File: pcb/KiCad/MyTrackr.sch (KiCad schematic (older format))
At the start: 41 parts, among them CN1 GPS_ANTENNA, CON1 MICRO_SD, J1 REGULATOR_3V3, J2 CONN_ICSP, J3 CONN_SERIAL, J4 CONN_BAT, P1 CONN_OLED, Q1 Q_PMOS_GSD, SW1 BTN_RESET, SW2 BTN_BACK, SW3 BTN_PREV, SW4 BTN_NEXT, SW5 BTN_SEL, U1 ATmega328P-AU, U2 GPS-NEO-6M, U3 24AA32

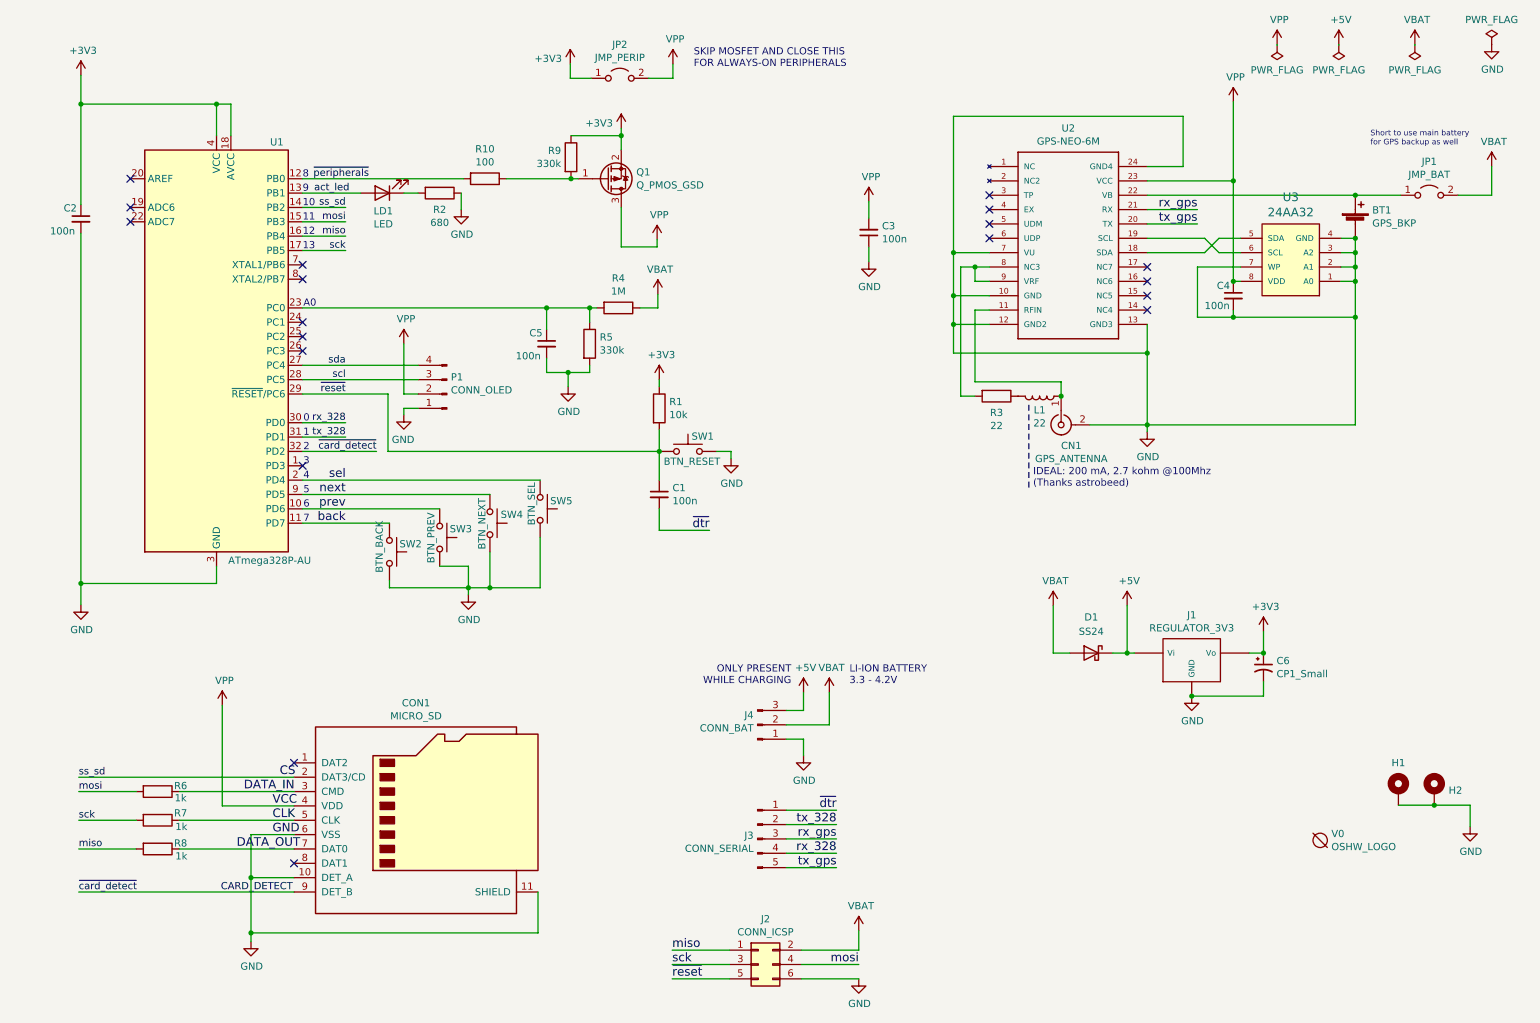
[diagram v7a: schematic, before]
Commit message: Add i2c pull-ups
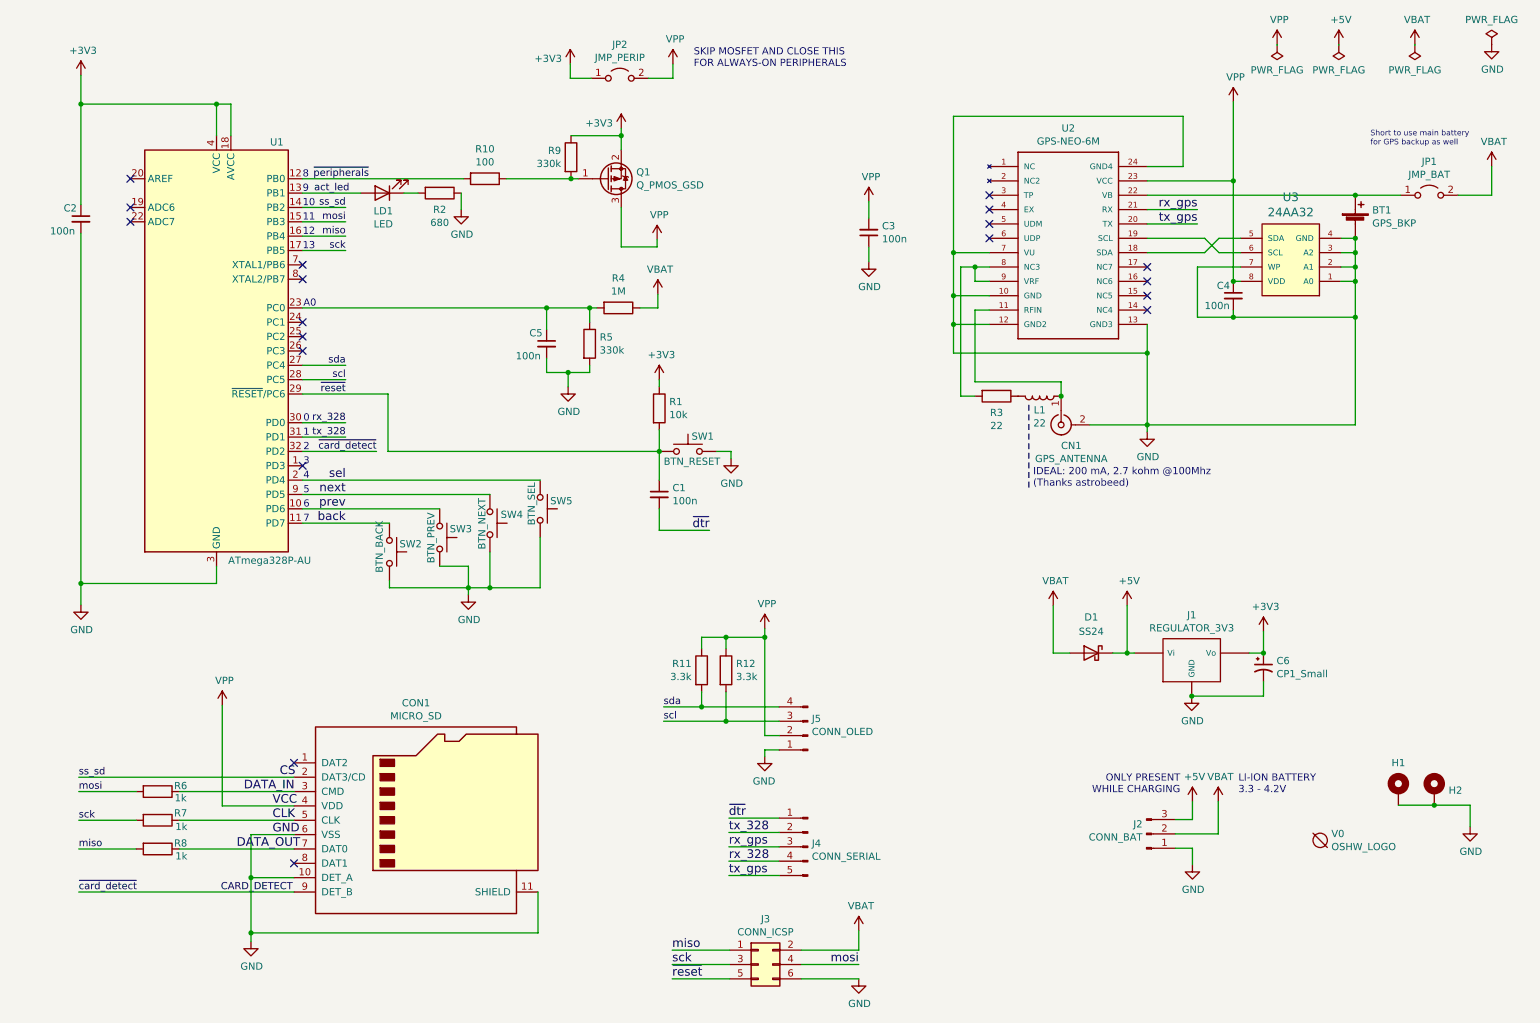
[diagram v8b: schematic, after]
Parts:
- added R11, R12: 3.3k, Resistor_SMD:R_0805_2012Metric_Pad1.20x1.40mm_HandSolder, symbol Device:R
- renumbered J4 to J2, J2 to J3, J3 to J4, P1 to J5
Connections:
- net VPP: now also R11.1, R12.1
- net scl: now also R12.2
- net sda: now also R11.2
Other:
- moved on the sheet: J2, J4, J5
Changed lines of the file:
@@
 Sheet 1 1
 Title "MyTrackr"
-Date "2021-01-10"
+Date "2021-01-14"
 Rev "2git"
 Comp "SukkoPera"
@@
 Text Label 8900 2050 2    60   ~ 0
 tx_gps
-Text Label 6385 6535 2    60   ~ 0
-tx_gps
-Text Label 6385 6435 2    60   ~ 0
-rx_328
-Text Label 6385 6335 2    60   ~ 0
-rx_gps
-Text Label 6385 6235 2    60   ~ 0
-tx_328
 Text Label 5500 4185 2    60   ~ 0
-~dtr
-Text Label 6385 6135 2    60   ~ 0
 ~dtr
 Text Label 2745 1835 0    50   ~ 0
@@
 	1505 6205 1105 6205
 Wire Wire Line
-	6385 6135 6035 6135
-Wire Wire Line
 	8550 2050 8900 2050
 Wire Wire Line
@@
 Wire Wire Line
 	4665 2635 4665 2735
-Wire Wire Line
-	3370 3335 3470 3335
 Connection ~ 10000 2700
 Connection ~ 5150 3635
@@
 	5150 4035 5150 4185
 Wire Wire Line
-	6385 6535 6035 6535
-Wire Wire Line
-	6385 6435 6035 6435
-Wire Wire Line
-	6385 6335 6035 6335
-Wire Wire Line
-	6385 6235 6035 6235
-Wire Wire Line
 	9360 5040 9360 4890
 Wire Wire Line
@@
 Wire Wire Line
 	2605 6305 2305 6305
-Wire Wire Line
-	3370 2885 3370 3235
 Wire Wire Line
 	1120 2115 1120 4555
@@
 $EndComp
 $Comp
-L Connector:Conn_01x03_Male J4
-U 1 1 60013045
-P 5835 5540
-F 0 "J4" H 5807 5472 50  0000 R CNN
-F 1 "CONN_BAT" H 5807 5563 50  0000 R CNN
-F 2 "Connector_PinHeader_2.54mm:PinHeader_1x03_P2.54mm_Vertical" H 5835 5540 50  0001 C CNN
-F 3 "~" H 5835 5540 50  0001 C CNN
-	1    5835 5540
-	1    0    0    1
-$EndComp
-$Comp
 L power:GND #PWR0106
 U 1 1 6003CA1E
@@
 $EndComp
 $Comp
-L Connector_Generic:Conn_02x03_Odd_Even J2
+L Connector_Generic:Conn_02x03_Odd_Even J3
 U 1 1 6005B0A6
 P 5840 7210
-F 0 "J2" H 5890 7527 50  0000 C CNN
+F 0 "J3" H 5890 7527 50  0000 C CNN
 F 1 "CONN_ICSP" H 5890 7436 50  0000 C CNN
 F 2 "Connector_PinHeader_2.54mm:PinHeader_2x03_P2.54mm_Vertical" H 5840 7210 50  0001 C CNN
@@
 $EndComp
 $Comp
-L Connector:Conn_01x04_Male P1
-U 1 1 601D5E73
-P 3670 3235
-F 0 "P1" H 3642 3117 50  0000 R CNN
-F 1 "CONN_OLED" H 3642 3208 50  0000 R CNN
-F 2 "Connector_PinHeader_2.54mm:PinHeader_1x04_P2.54mm_Vertical" H 3670 3235 50  0001 C CNN
-F 3 "~" H 3670 3235 50  0001 C CNN
-	1    3670 3235
-	-1   0    0    1
-$EndComp
-$Comp
 L Switch:SW_Push SW3
 U 1 1 601EEEB4
@@
 	1    4320 4035
 	0    1    1    0
-$EndComp
-$Comp
-L Connector:Conn_01x05_Male J3
-U 1 1 60211901
-P 5835 6335
-F 0 "J3" H 5807 6359 50  0000 R CNN
-F 1 "CONN_SERIAL" H 5807 6268 50  0000 R CNN
-F 2 "Connector_PinHeader_2.54mm:PinHeader_1x05_P2.54mm_Vertical" H 5835 6335 50  0001 C CNN
-F 3 "~" H 5835 6335 50  0001 C CNN
-	1    5835 6335
-	1    0    0    -1
 $EndComp
 $Comp
@@
 F 3 "" H 3820 4635 50  0001 C CNN
 	1    3820 4635
-	1    0    0    -1
-$EndComp
-$Comp
-L power:VPP #PWR0116
-U 1 1 60568F57
-P 3370 2885
-F 0 "#PWR0116" H 3370 2735 50  0001 C CNN
-F 1 "VPP" H 3385 3058 50  0000 C CNN
-F 2 "" H 3370 2885 50  0001 C CNN
-F 3 "" H 3370 2885 50  0001 C CNN
-	1    3370 2885
 	1    0    0    -1
 $EndComp
@@
 sda
 Wire Wire Line
-	2665 3135 3470 3135
-Wire Wire Line
-	2665 3035 3470 3035
-Wire Wire Line
-	3370 3235 3470 3235
-Wire Wire Line
 	2665 3435 2965 3435
 Wire Wire Line
@@
 Text Notes 2670 2635 0    50   ~ 0
 A0
-$Comp
-L power:GND #PWR0115
-U 1 1 6055ECA2
-P 3370 3380
-F 0 "#PWR0115" H 3370 3130 50  0001 C CNN
-F 1 "GND" H 3375 3207 50  0000 C CNN
-F 2 "" H 3370 3380 50  0001 C CNN
-F 3 "" H 3370 3380 50  0001 C CNN
-	1    3370 3380
-	-1   0    0    -1
-$EndComp
-Wire Wire Line
-	3370 3380 3370 3335
 Connection ~ 3970 4585
 Wire Wire Line
@@
 Wire Wire Line
 	5140 2540 5140 2635
-Wire Wire Line
-	6035 5640 6155 5640
-Wire Wire Line
-	6155 5640 6155 5755
-Wire Wire Line
-	6035 5440 6155 5440
-Wire Wire Line
-	6155 5440 6155 5315
-Wire Wire Line
-	6035 5540 6335 5540
-Wire Wire Line
-	6335 5540 6335 5315
-$Comp
-L MyTrackr:VBAT #PWR0126
-U 1 1 6054073A
-P 6335 5315
-F 0 "#PWR0126" H 6335 5165 50  0001 C CNN
-F 1 "VBAT" H 6350 5488 50  0000 C CNN
-F 2 "" H 6335 5315 50  0001 C CNN
-F 3 "" H 6335 5315 50  0001 C CNN
-	1    6335 5315
-	1    0    0    -1
-$EndComp
-$Comp
-L power:+5V #PWR0127
-U 1 1 60541662
-P 6155 5315
-F 0 "#PWR0127" H 6155 5165 50  0001 C CNN
-F 1 "+5V" H 6170 5488 50  0000 C CNN
-F 2 "" H 6155 5315 50  0001 C CNN
-F 3 "" H 6155 5315 50  0001 C CNN
-	1    6155 5315
-	1    0    0    -1
-$EndComp
-$Comp
-L power:GND #PWR0128
-U 1 1 60541AAE
-P 6155 5755
-F 0 "#PWR0128" H 6155 5505 50  0001 C CNN
-F 1 "GND" H 6160 5582 50  0000 C CNN
-F 2 "" H 6155 5755 50  0001 C CNN
-F 3 "" H 6155 5755 50  0001 C CNN
-	1    6155 5755
-	1    0    0    -1
-$EndComp
-Text Notes 6475 5265 0    50   ~ 0
-LI-ION BATTERY\n3.3 - 4.2V
-Text Notes 6070 5265 2    50   ~ 0
-ONLY PRESENT\nWHILE CHARGING
 $Comp
 L power:+5V #PWR0129
@@
 Text Notes 5390 965  0    50   ~ 0
 SKIP MOSFET AND CLOSE THIS\nFOR ALWAYS-ON PERIPHERALS
+Wire Wire Line
+	2665 3035 2965 3035
+Wire Wire Line
+	2665 3135 2965 3135
+$Comp
+L Connector:Conn_01x03_Male J2
+U 1 1 60013045
+P 8545 6300
+F 0 "J2" H 8517 6232 50  0000 R CNN
+F 1 "CONN_BAT" H 8517 6323 50  0000 R CNN
+F 2 "Connector_PinHeader_2.54mm:PinHeader_1x03_P2.54mm_Vertical" H 8545 6300 50  0001 C CNN
+F 3 "~" H 8545 6300 50  0001 C CNN
+	1    8545 6300
+	1    0    0    1
+$EndComp
+Wire Wire Line
+	8745 6400 8865 6400
+Wire Wire Line
+	8865 6400 8865 6515
+Wire Wire Line
+	8745 6200 8865 6200
+Wire Wire Line
+	8865 6200 8865 6075
+Wire Wire Line
+	8745 6300 9045 6300
+Wire Wire Line
+	9045 6300 9045 6075
+$Comp
+L MyTrackr:VBAT #PWR0126
+U 1 1 6054073A
+P 9045 6075
+F 0 "#PWR0126" H 9045 5925 50  0001 C CNN
+F 1 "VBAT" H 9060 6248 50  0000 C CNN
+F 2 "" H 9045 6075 50  0001 C CNN
+F 3 "" H 9045 6075 50  0001 C CNN
+	1    9045 6075
+	1    0    0    -1
+$EndComp
+$Comp
+L power:+5V #PWR0127
+U 1 1 60541662
+P 8865 6075
+F 0 "#PWR0127" H 8865 5925 50  0001 C CNN
+F 1 "+5V" H 8880 6248 50  0000 C CNN
+F 2 "" H 8865 6075 50  0001 C CNN
+F 3 "" H 8865 6075 50  0001 C CNN
+	1    8865 6075
+	1    0    0    -1
+$EndComp
+$Comp
+L power:GND #PWR0128
+U 1 1 60541AAE
+P 8865 6515
+F 0 "#PWR0128" H 8865 6265 50  0001 C CNN
+F 1 "GND" H 8870 6342 50  0000 C CNN
+F 2 "" H 8865 6515 50  0001 C CNN
+F 3 "" H 8865 6515 50  0001 C CNN
+	1    8865 6515
+	1    0    0    -1
+$EndComp
+Text Notes 9185 6025 0    50   ~ 0
+LI-ION BATTERY\n3.3 - 4.2V
+Text Notes 8780 6025 2    50   ~ 0
+ONLY PRESENT\nWHILE CHARGING
+Text Label 5635 6590 0    60   ~ 0
+tx_gps
+Text Label 5635 6490 0    60   ~ 0
+rx_328
+Text Label 5635 6390 0    60   ~ 0
+rx_gps
+Text Label 5635 6290 0    60   ~ 0
+tx_328
+Text Label 5635 6190 0    60   ~ 0
+~dtr
+Wire Wire Line
+	5635 6190 5985 6190
+Wire Wire Line
+	5635 6590 5985 6590
+Wire Wire Line
+	5635 6490 5985 6490
+Wire Wire Line
+	5635 6390 5985 6390
+Wire Wire Line
+	5635 6290 5985 6290
+$Comp
+L Connector:Conn_01x05_Male J4
+U 1 1 60211901
+P 6185 6390
+F 0 "J4" H 6157 6414 50  0000 R CNN
+F 1 "CONN_SERIAL" H 6157 6323 50  0000 R CNN
+F 2 "Connector_PinHeader_2.54mm:PinHeader_1x05_P2.54mm_Vertical" H 6185 6390 50  0001 C CNN
+F 3 "~" H 6185 6390 50  0001 C CNN
+	1    6185 6390
+	-1   0    0    -1
+$EndComp
+Wire Wire Line
+	5885 5715 5985 5715
+$Comp
+L Connector:Conn_01x04_Male J5
+U 1 1 601D5E73
+P 6185 5615
+F 0 "J5" H 6157 5497 50  0000 R CNN
+F 1 "CONN_OLED" H 6157 5588 50  0000 R CNN
+F 2 "Connector_PinHeader_2.54mm:PinHeader_1x04_P2.54mm_Vertical" H 6185 5615 50  0001 C CNN
+F 3 "~" H 6185 5615 50  0001 C CNN
+	1    6185 5615
+	-1   0    0    1
+$EndComp
+Wire Wire Line
+	5180 5515 5615 5515
+Wire Wire Line
+	5180 5415 5445 5415
+Wire Wire Line
+	5885 5615 5985 5615
+$Comp
+L power:GND #PWR0115
+U 1 1 6055ECA2
+P 5885 5760
+F 0 "#PWR0115" H 5885 5510 50  0001 C CNN
+F 1 "GND" H 5890 5587 50  0000 C CNN
+F 2 "" H 5885 5760 50  0001 C CNN
+F 3 "" H 5885 5760 50  0001 C CNN
+	1    5885 5760
+	-1   0    0    -1
+$EndComp
+Wire Wire Line
+	5885 5760 5885 5715
+$Comp
+L power:VPP #PWR0116
+U 1 1 60568F57
+P 5885 4870
+F 0 "#PWR0116" H 5885 4720 50  0001 C CNN
+F 1 "VPP" H 5900 5043 50  0000 C CNN
+F 2 "" H 5885 4870 50  0001 C CNN
+F 3 "" H 5885 4870 50  0001 C CNN
+	1    5885 4870
+	1    0    0    -1
+$EndComp
+Text Label 5180 5415 0    50   ~ 0
+sda
+Text Label 5180 5515 0    50   ~ 0
+scl
+$Comp
+L Device:R R11
+U 1 1 60746F65
+P 5445 5160
+F 0 "R11" H 5375 5206 50  0000 R CNN
+F 1 "3.3k" H 5375 5115 50  0000 R CNN
+F 2 "Resistor_SMD:R_0805_2012Metric_Pad1.20x1.40mm_HandSolder" V 5375 5160 50  0001 C CNN
+F 3 "~" H 5445 5160 50  0001 C CNN
+	1    5445 5160
+	1    0    0    -1
+$EndComp
+$Comp
+L Device:R R12
+U 1 1 60747A79
+P 5615 5160
+F 0 "R12" H 5685 5206 50  0000 L CNN
+F 1 "3.3k" H 5685 5115 50  0000 L CNN
+F 2 "Resistor_SMD:R_0805_2012Metric_Pad1.20x1.40mm_HandSolder" V 5545 5160 50  0001 C CNN
+F 3 "~" H 5615 5160 50  0001 C CNN
+	1    5615 5160
+	1    0    0    -1
+$EndComp
+Wire Wire Line
+	5885 4870 5885 4930
+Wire Wire Line
+	5445 5310 5445 5415
+Connection ~ 5445 5415
+Wire Wire Line
+	5445 5415 5985 5415
+Wire Wire Line
+	5615 5310 5615 5515
+Connection ~ 5615 5515
+Wire Wire Line
+	5615 5515 5985 5515
+Wire Wire Line
+	5615 5010 5615 4930
+Wire Wire Line
+	5615 4930 5885 4930
+Connection ~ 5885 4930
+Wire Wire Line
+	5885 4930 5885 5615
+Wire Wire Line
+	5445 5010 5445 4930
+Wire Wire Line
+	5445 4930 5615 4930
+Connection ~ 5615 4930
 $EndSCHEMATC
